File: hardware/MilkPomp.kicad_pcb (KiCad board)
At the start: 2 copper layers, 74 parts, among them J1 Screw_Terminal_01x04, J2 BOOT, J3 Conn_01x04_Male, J4 Conn_Board, J5 Conn_Display, K1 G5LE-1, Q1 BC847, SW1 SW_IO, SW2 SW_START, SW3 SW_MODE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

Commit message: milkpomp pcb continued
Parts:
- moved Q1 198.2 mm to (41.7, 111.8)
- moved K1 197.0 mm to (55.4, 109.8)
- moved R16 193.9 mm to (37.6, 111.9), turned to -90 degrees
- moved R15 193.3 mm to (37.6, 108.2), turned to -90 degrees
- moved D2 188.6 mm to (42.8, 103.4)
- moved R14 185.3 mm to (47.5, 103.4)
- moved D3 175.4 mm to (59.4, 103.2), turned to 180 degrees
- moved D1 98.4 mm to (91.4, 127.0), turned to -90 degrees
- moved C11 85.7 mm to (198.1, 86.4), turned to 180 degrees
- moved R3 83.9 mm to (204.9, 85.7), turned to -90 degrees
- moved Y2 83.6 mm to (193.3, 81.2), turned to 180 degrees
- moved R21 78.3 mm to (88.9, 136.1), turned to -90 degrees
- moved C4 76.5 mm to (188.0, 86.4), turned to -90 degrees
- moved C9 73.8 mm to (188.3, 75.6), turned to 90 degrees
- moved U4 72.9 mm to (96.5, 136.3)
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
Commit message: PCB designed
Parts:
- added J6: PWR INPUT, Connector_Phoenix_MC:PhoenixContact_MC_1,5_2-G-3.81_1x02_P3.81mm_Horizontal, F.Cu at (23.6, 144.2)
- moved H2 272.2 mm to (32.8, 160.3)
- moved H1 247.2 mm to (33.1, 110.1)
- moved H4 230.3 mm to (75.9, 160.3)
- moved J5 220.7 mm to (137.3, 152.8)
- moved R13 220.7 mm to (206.3, 141.1)
- moved R6 220.7 mm to (206.3, 133.5)
- moved R7 220.7 mm to (206.3, 136.0)
- moved R8 220.7 mm to (206.3, 138.6)
- moved R10 220.7 mm to (193.8, 141.1)
- moved R11 220.7 mm to (193.8, 136.0)
- moved R12 220.7 mm to (193.8, 138.6)
- moved R9 220.7 mm to (193.8, 143.7)
- moved U3 220.7 mm to (197.4, 133.5)
- moved C12 220.7 mm to (167.6, 125.8)
- moved C13 220.7 mm to (167.6, 140.4)
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
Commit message: PCB designed2
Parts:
- moved H3 0.89 mm to (76.3, 109.1)
- moved LS1 0.89 mm to (93.2, 113.9)
- moved H1 0.89 mm to (33.2, 109.2)
- moved H5 0.89 mm to (116.0, 109.2)
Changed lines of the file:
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@@
   )
   (footprint "Buzzer:XDCR_KPEG228" (layer "F.Cu")
-    (at 93.1164 114.808 90)
+    (at 93.1672 113.9164 90)
     (property "MANUFACTURER" "Kingstate")
     (property "MAXIMUM_PACKAGE_HEIGHT" "9 mm")
@@
   )
   (footprint "MountingHole:MountingHole_2.5mm" (layer "F.Cu")
-    (at 33.1216 110.1344)
+    (at 33.1724 109.2428)
     (descr "Mounting Hole 2.5mm, no annular")
     (tags "mounting hole 2.5mm no annular")
@@
   )
   (footprint "MountingHole:MountingHole_2.5mm" (layer "F.Cu")
-    (at 115.9764 110.1344)
+    (at 116.0272 109.2428)
     (descr "Mounting Hole 2.5mm, no annular")
     (tags "mounting hole 2.5mm no annular")
@@
   )
   (footprint "MountingHole:MountingHole_2.5mm" (layer "F.Cu")
-    (at 76.2508 110.01)
+    (at 76.3016 109.1184)
     (descr "Mounting Hole 2.5mm, no annular")
     (tags "mounting hole 2.5mm no annular")

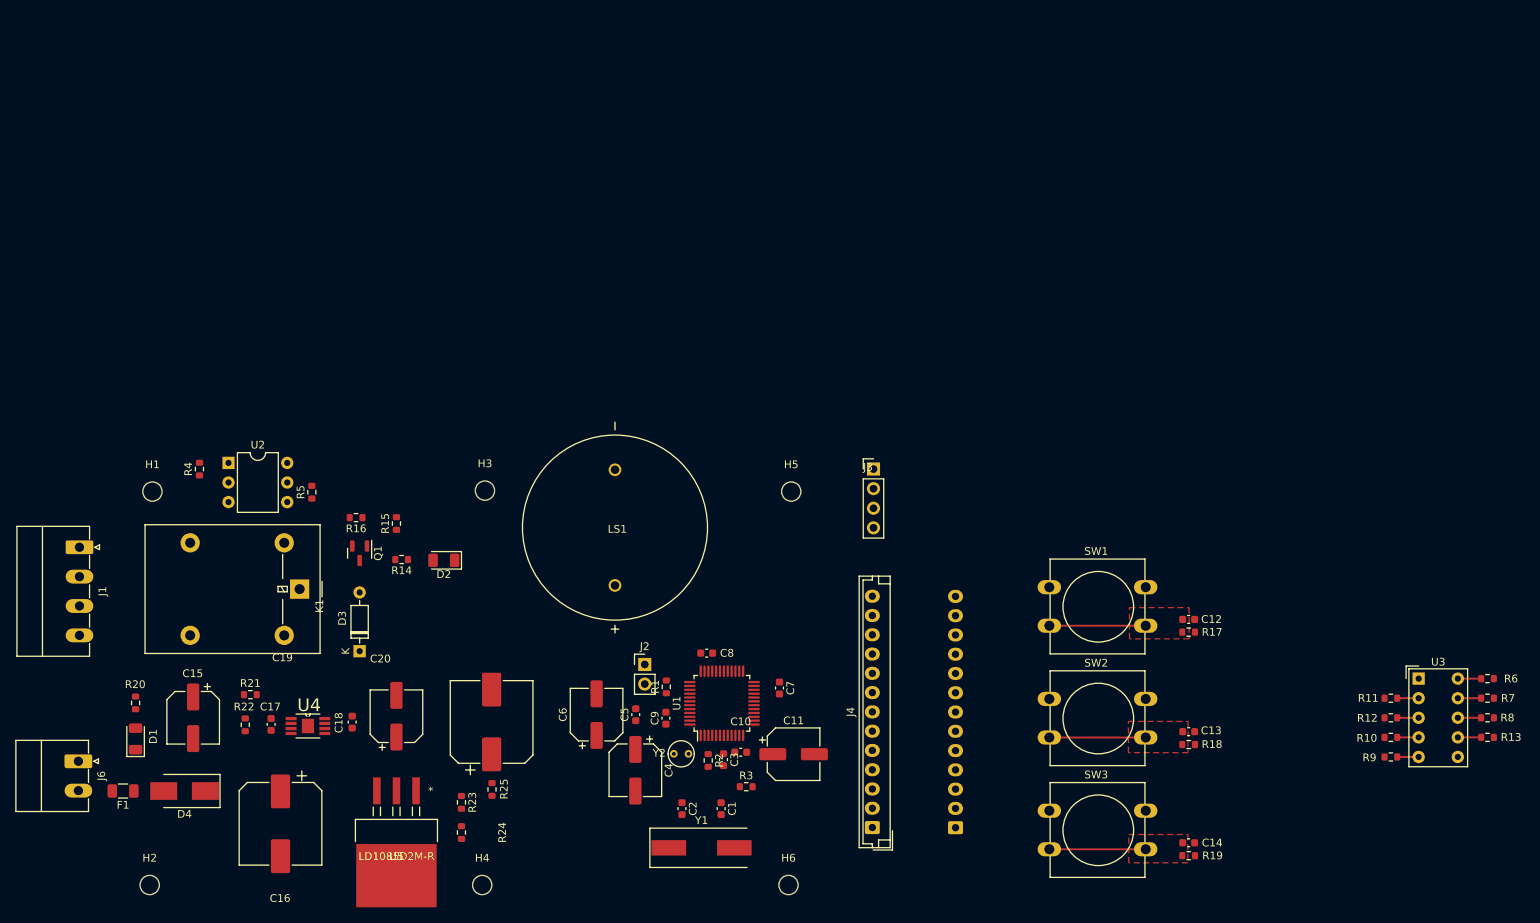
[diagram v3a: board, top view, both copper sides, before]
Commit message: Footprints are assigned and Cut edges fixed
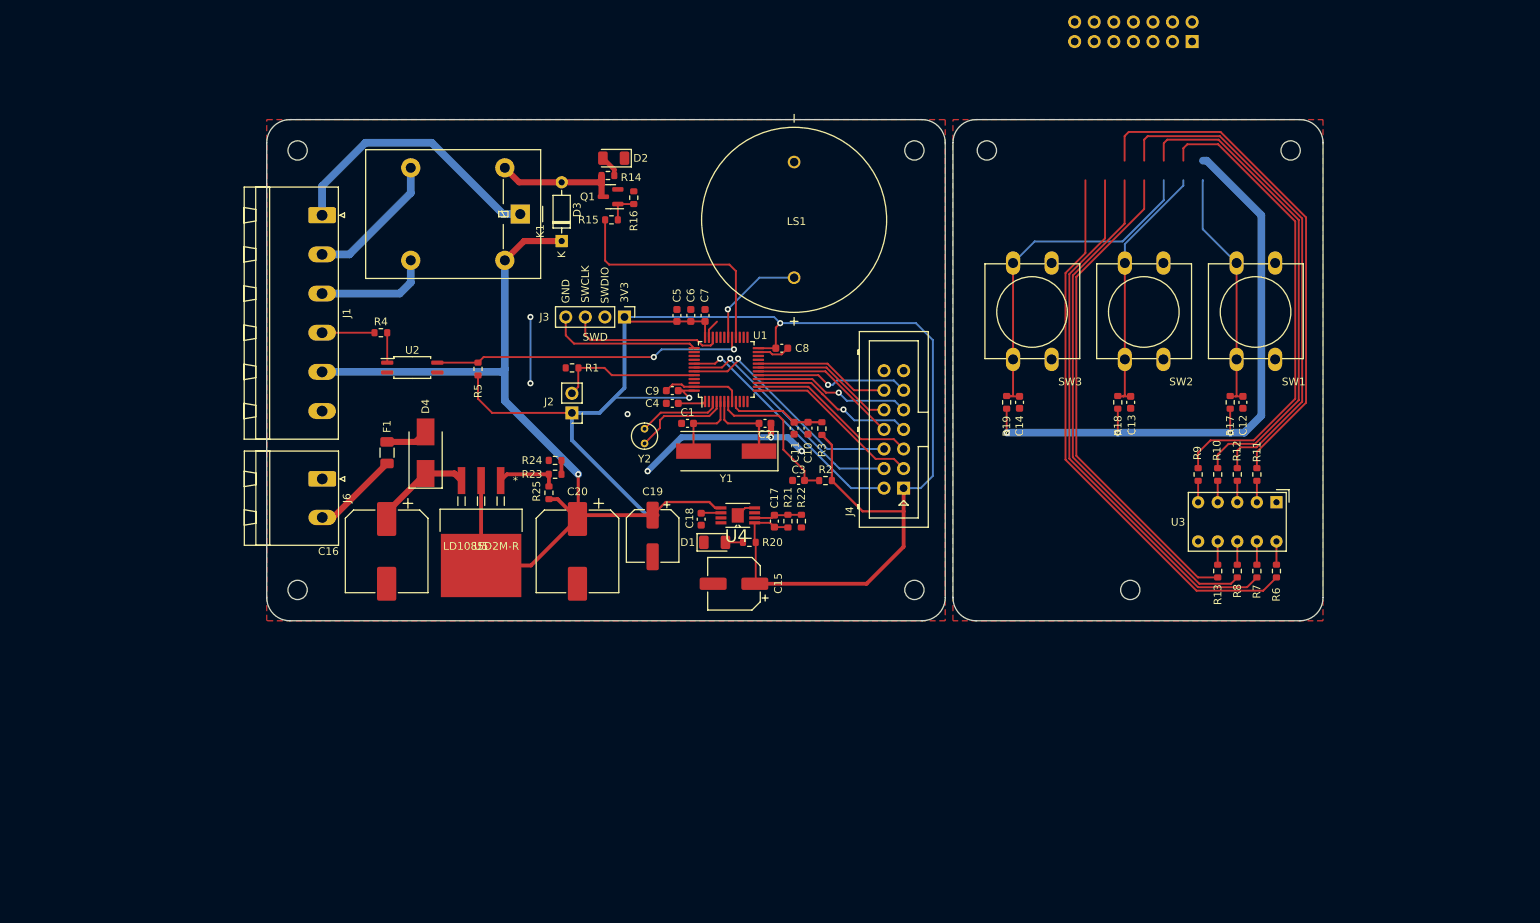
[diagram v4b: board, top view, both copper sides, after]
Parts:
- added H7: MountingHole, MountingHole:MountingHole_2.5mm, F.Cu at (141.4, 65.0)
- C11, C4, C6: footprint Capacitor_SMD:CP_Elec_6.3x7.7 -> Capacitor_SMD:C_0603_1608Metric
- J1: value Screw_Terminal_01x04 -> Screw_Terminal_01x06; footprint Connector_Phoenix_MC:PhoenixContact_MC_1,5_4-G-3.81_1x04_P3.81mm_Horizontal -> Connector_Phoenix_MSTB:PhoenixContact_MSTBA_2,5_6-G-5,08_1x06_P5.08mm_Horizontal
- J4, J5: footprint Connector_JST:JST_EH_B13B-EH-A_1x13_P2.50mm_Vertical -> Connector_Multicomp:Multicomp_MC9A12-1434_2x07x2.54mm_Straight
- J6: footprint Connector_Phoenix_MC:PhoenixContact_MC_1,5_2-G-3.81_1x02_P3.81mm_Horizontal -> Connector_Phoenix_MSTB:PhoenixContact_MSTBA_2,5_2-G_1x02_P5.00mm_Horizontal
- R4: value 1K -> 3K3
- U2: value 4N25 -> TLP291; footprint Package_DIP:DIP-6_W7.62mm -> Package_SO:SOIC-4_4.55x2.6mm_P1.27mm
- moved H6 115.4 mm to (180.8, 65.0), turned to -90 degrees
- moved J5 106.5 mm to (168.0, 50.9), turned to 180 degrees
- moved R20 82.3 mm to (110.6, 115.8), turned to 180 degrees
- moved D1 79.3 mm to (106.1, 115.8), turned to 0 degrees
- moved R22 76.8 mm to (117.3, 113.1), turned to -90 degrees
- moved R21 73.3 mm to (115.6, 113.1), turned to 90 degrees
- moved C15 72.3 mm to (108.6, 121.2), turned to 180 degrees
- moved H3 71.1 mm to (132.0, 65.0)
- moved SW3 71.0 mm to (149.8, 79.6), turned to -90 degrees
- moved C17 70.4 mm to (113.8, 113.1), turned to 90 degrees
- moved H4 67.9 mm to (132.0, 122.0)
- moved R19 63.4 mm to (144.0, 97.7), turned to 90 degrees
- moved U4 62.1 mm to (109.1, 112.3), turned to 180 degrees
- moved C14 61.2 mm to (145.6, 97.7), turned to -90 degrees
- moved D3 59.3 mm to (86.2, 76.8)
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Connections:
- net VCC renamed /Power/VCC
- J1 pad 1: /Flow/FLOW_SENSOR -> /Relay/RELAY_IN
- J1 pad 2: /Relay/RELAY_IN -> /Relay/RELAY_NO
- J1 pad 3: /Relay/RELAY_NO -> /Relay/RELAY_NC
- J1 pad 4: /Relay/RELAY_NC -> /Flow/FLOW_SENSOR
- J3 pad 2: SWDIO -> GND
- J3 pad 3: SWCLK -> SWDIO
- J3 pad 4: GND -> SWCLK
- J4 pad 10: DISP_F -> DISP_G
- J4 pad 11: DISP_G -> DISP_E
- J4 pad 3: BTN_START -> DISP_A
- J4 pad 4: BTN_MODE -> BTN_START
- J4 pad 5: DISP_A -> DISP_B
- J4 pad 6: DISP_B -> BTN_MODE
- J4 pad 8: DISP_D -> DISP_F
- J4 pad 9: DISP_E -> DISP_D
- J5 pad 10: /DISPLAY/DISP_F -> /DISPLAY/DISP_C
- J5 pad 11: /DISPLAY/DISP_G -> unconnected-(J5-Pad11)
- J5 pad 12: /DISPLAY/DISP_P -> /DISPLAY/DISP_B
- J5 pad 2: /Buttons/BTN_IO -> unconnected-(J5-Pad2)
- J5 pad 3: /Buttons/BTN_START -> /DISPLAY/DISP_D
- J5 pad 4: /Buttons/BTN_MODE -> unconnected-(J5-Pad4)
- J5 pad 5: /DISPLAY/DISP_A -> /DISPLAY/DISP_E
- J5 pad 6: /DISPLAY/DISP_B -> unconnected-(J5-Pad6)
- J5 pad 7: /DISPLAY/DISP_C -> /DISPLAY/DISP_G
- J5 pad 8: /DISPLAY/DISP_D -> /DISPLAY/DISP_P
- J5 pad 9: /DISPLAY/DISP_E -> /DISPLAY/DISP_F
- R17 pad 1: +3.3V -> +3V3
- R18 pad 1: +3.3V -> +3V3
- R19 pad 1: +3.3V -> +3V3
- U2 pad 3: unconnected-(U2-Pad3) -> GND
- U2 pad 4: GND -> FLOW
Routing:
- net +3V3: track 0.00 -> 292.2 mm, vias 0 -> 5
- net +12V: track 0.00 -> 121.1 mm, vias 0 -> 1
- net /DISPLAY/DISP_A: track 0.00 -> 72.4 mm
- net /DISPLAY/DISP_B: track 0.00 -> 69.8 mm
- net /DISPLAY/DISP_C: track 0.00 -> 67.2 mm
- net /DISPLAY/DISP_F: track 0.00 -> 66.7 mm
- net /DISPLAY/DISP_G: track 0.00 -> 64.9 mm
- net /DISPLAY/DISP_P: track 0.00 -> 64.3 mm
- net /DISPLAY/DISP_E: track 0.00 -> 62.8 mm
- net /DISPLAY/DISP_D: track 0.00 -> 61.0 mm
- net GND: track 0.00 -> 52.9 mm, vias 0 -> 6
- net FLOW: track 0.00 -> 40.9 mm, vias 0 -> 2
- net /Relay/RELAY_IN: track 0.00 -> 35.6 mm
- net /Buttons/BTN_MODE: track 12.5 -> 46.1 mm
- net BTN_IO: track 0.00 -> 31.9 mm, vias 0 -> 1
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- added copper zone on F.Cu, net GND
- removed copper zone on F.Cu, net /Buttons/BTN_IO
- removed copper zone on F.Cu, net /Buttons/BTN_MODE
- removed copper zone on F.Cu, net /Buttons/BTN_START
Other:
- board outline added: 137 x 65 mm
- board text added: "3V3"
- board text added: "GND"
- board text added: "SWCLK"
- board text added: "SWD"
- board text added: "SWDIO"

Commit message: PCB drawing completed
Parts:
- moved R18 48.9 mm to (205.0, 112.4), turned to 180 degrees
- moved R19 48.7 mm to (190.4, 112.4), turned to 180 degrees
- moved R17 48.6 mm to (219.2, 112.4), turned to 180 degrees
- moved C15 46.3 mm to (151.6, 138.3)
- moved C3 46.3 mm to (160.0, 124.9)
- moved C4 46.3 mm to (143.6, 114.9)
- moved D2 46.3 mm to (136.0, 83.1)
- moved D3 46.3 mm to (129.3, 93.8)
- moved D4 46.3 mm to (111.6, 121.3)
- moved H1 46.3 mm to (95.0, 82.1)
- moved H3 46.3 mm to (175.0, 82.1)
- moved H7 46.3 mm to (184.4, 82.1)
- moved J2 46.3 mm to (130.6, 116.1)
- moved J3 46.3 mm to (137.4, 103.7)
- moved J4 46.3 mm to (173.6, 125.9)
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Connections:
- J4 pad 1: +3V3 -> GND
- J4 pad 10: DISP_G -> DISP_B
- J4 pad 11: DISP_E -> DISP_D
- J4 pad 12: DISP_P -> DISP_C
- J4 pad 13: GND -> +3V3
- J4 pad 14: GND -> DISP_P
- J4 pad 2: BTN_IO -> BTN_MODE
- J4 pad 3: DISP_A -> GND
- J4 pad 5: DISP_B -> DISP_F
- J4 pad 6: BTN_MODE -> BTN_IO
- J4 pad 7: DISP_C -> DISP_G
- J4 pad 8: DISP_F -> DISP_A
- J4 pad 9: DISP_D -> DISP_E
- J5 pad 1: +3V3 -> GND
- J5 pad 10: /DISPLAY/DISP_C -> /DISPLAY/DISP_B
- J5 pad 11: unconnected-(J5-Pad11) -> /DISPLAY/DISP_D
- J5 pad 12: /DISPLAY/DISP_B -> /DISPLAY/DISP_C
- J5 pad 13: GND -> +3V3
- J5 pad 14: /DISPLAY/DISP_A -> /DISPLAY/DISP_P
- J5 pad 2: unconnected-(J5-Pad2) -> /Buttons/BTN_MODE
- J5 pad 3: /DISPLAY/DISP_D -> GND
- J5 pad 4: unconnected-(J5-Pad4) -> /Buttons/BTN_START
- J5 pad 5: /DISPLAY/DISP_E -> /DISPLAY/DISP_F
- J5 pad 6: unconnected-(J5-Pad6) -> /Buttons/BTN_IO
- J5 pad 8: /DISPLAY/DISP_P -> /DISPLAY/DISP_A
- J5 pad 9: /DISPLAY/DISP_F -> /DISPLAY/DISP_E
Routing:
- net /Buttons/BTN_MODE: track 46.1 -> 30.6 mm
- net +3V3: track 292.2 -> 279.9 mm, vias 5 -> 4
- net DISP_F: track 19.4 -> 31.1 mm, vias 0 -> 2
- net /Buttons/BTN_IO: track 31.6 -> 41.8 mm
- net DISP_G: track 18.6 -> 28.5 mm
- net GND: track 52.9 -> 57.6 mm
- net DISP_A: track 23.0 -> 18.4 mm
- net DISP_B: track 22.2 -> 18.3 mm
- net /DISPLAY/DISP_P: track 64.3 -> 67.1 mm
- net DISP_C: track 21.5 -> 18.8 mm, vias 1 -> 0
- net DISP_E: track 20.1 -> 22.6 mm
- net /DISPLAY/DISP_C: track 67.2 -> 69.5 mm
- net BTN_IO: track 31.9 -> 29.9 mm
- net /DISPLAY/DISP_B: track 69.8 -> 71.5 mm
- net /DISPLAY/DISP_E: track 62.8 -> 64.3 mm
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
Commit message: All PCB drawing completed
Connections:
- J4 pad 1: GND -> +3V3
- J4 pad 3: GND -> +3V3
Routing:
- net +3V3: track 279.9 -> 283.4 mm
- net /Buttons/BTN_MODE: track 30.6 -> 33.9 mm
- net /DISPLAY/DISP_A: track 73.8 -> 77.0 mm
- net /Buttons/BTN_START: track 31.7 -> 33.8 mm
- net /DISPLAY/DISP_B: track 71.5 -> 73.2 mm
- net GND: track 57.6 -> 55.9 mm
- net /DISPLAY/DISP_D: track 62.4 -> 60.8 mm
- net /DISPLAY/DISP_P: track 67.1 -> 65.7 mm
- net /Buttons/BTN_IO: track 41.8 -> 42.9 mm
- net /DISPLAY/DISP_E: track 64.3 -> 63.2 mm
- net /Power/VCC: track 11.3 -> 12.1 mm
- net /DISPLAY/DISP_F: track 67.8 -> 68.5 mm

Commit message: PCB design completed
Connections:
- J4 pad 1: +3V3 -> GND
- J4 pad 3: +3V3 -> GND
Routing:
- net GND: track 55.9 -> 66.4 mm, vias 6 -> 9
- net +3V3: track 283.4 -> 291.2 mm
- net /DISPLAY/DISP_D: track 60.8 -> 58.9 mm
- net /DISPLAY/DISP_E: track 63.2 -> 61.5 mm
- net /DISPLAY/DISP_G: track 66.1 -> 64.7 mm
- net /DISPLAY/DISP_F: track 68.5 -> 67.5 mm

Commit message: All PCB design completed
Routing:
- net GND: vias 9 -> 18
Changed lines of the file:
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@@
   (via (at 140.4104 123.6844) (size 0.8) (drill 0.4) (layers "F.Cu" "B.Cu") (net 1))
   (via (at 210.566 90.9828) (size 0.8) (drill 0.4) (layers "F.Cu" "B.Cu") (free) (net 1))
+  (via (at 103.9876 115.062) (size 0.8) (drill 0.4) (layers "F.Cu" "B.Cu") (free) (net 1))
+  (via (at 205.9432 121.2088) (size 0.8) (drill 0.4) (layers "F.Cu" "B.Cu") (free) (net 1))
+  (via (at 144.4752 87.5792) (size 0.8) (drill 0.4) (layers "F.Cu" "B.Cu") (free) (net 1))
   (via (at 160.4104 121.0844) (size 0.8) (drill 0.4) (layers "F.Cu" "B.Cu") (free) (net 1))
   (via (at 137.8104 116.2844) (size 0.8) (drill 0.4) (layers "F.Cu" "B.Cu") (free) (net 1))
+  (via (at 187.452 120.4976) (size 0.8) (drill 0.4) (layers "F.Cu" "B.Cu") (free) (net 1))
   (via (at 149.4028 101.092) (size 0.8) (drill 0.4) (layers "F.Cu" "B.Cu") (net 1))
+  (via (at 116.4336 102.7684) (size 0.8) (drill 0.4) (layers "F.Cu" "B.Cu") (free) (net 1))
+  (via (at 141.3256 139.1412) (size 0.8) (drill 0.4) (layers "F.Cu" "B.Cu") (free) (net 1))
   (via (at 156.4104 119.2844) (size 0.8) (drill 0.4) (layers "F.Cu" "B.Cu") (free) (net 1))
   (via (at 215.2904 92.0496) (size 0.8) (drill 0.4) (layers "F.Cu" "B.Cu") (free) (net 1))
+  (via (at 171.8564 99.6188) (size 0.8) (drill 0.4) (layers "F.Cu" "B.Cu") (free) (net 1))
   (via (at 125.2104 112.2844) (size 0.8) (drill 0.4) (layers "F.Cu" "B.Cu") (free) (net 1))
+  (via (at 190.8048 133.096) (size 0.8) (drill 0.4) (layers "F.Cu" "B.Cu") (free) (net 1))
+  (via (at 169.3672 133.5532) (size 0.8) (drill 0.4) (layers "F.Cu" "B.Cu") (free) (net 1))
   (via (at 125.2104 103.6844) (size 0.8) (drill 0.4) (layers "F.Cu" "B.Cu") (free) (net 1))
   (segment (start 156.4104 119.2844) (end 144.8104 119.2844) (width 0.8) (layer "B.Cu") (net 1))
